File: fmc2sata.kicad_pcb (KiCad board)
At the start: 4 copper layers, 105 x 69 mm, 40 parts, among them J1 ASP-134488-01, J2 1-2199230-6, J3 te-770829-1, U1 TPS565208, U2 TPS565208, Y1 AX3DAF1-150.0000

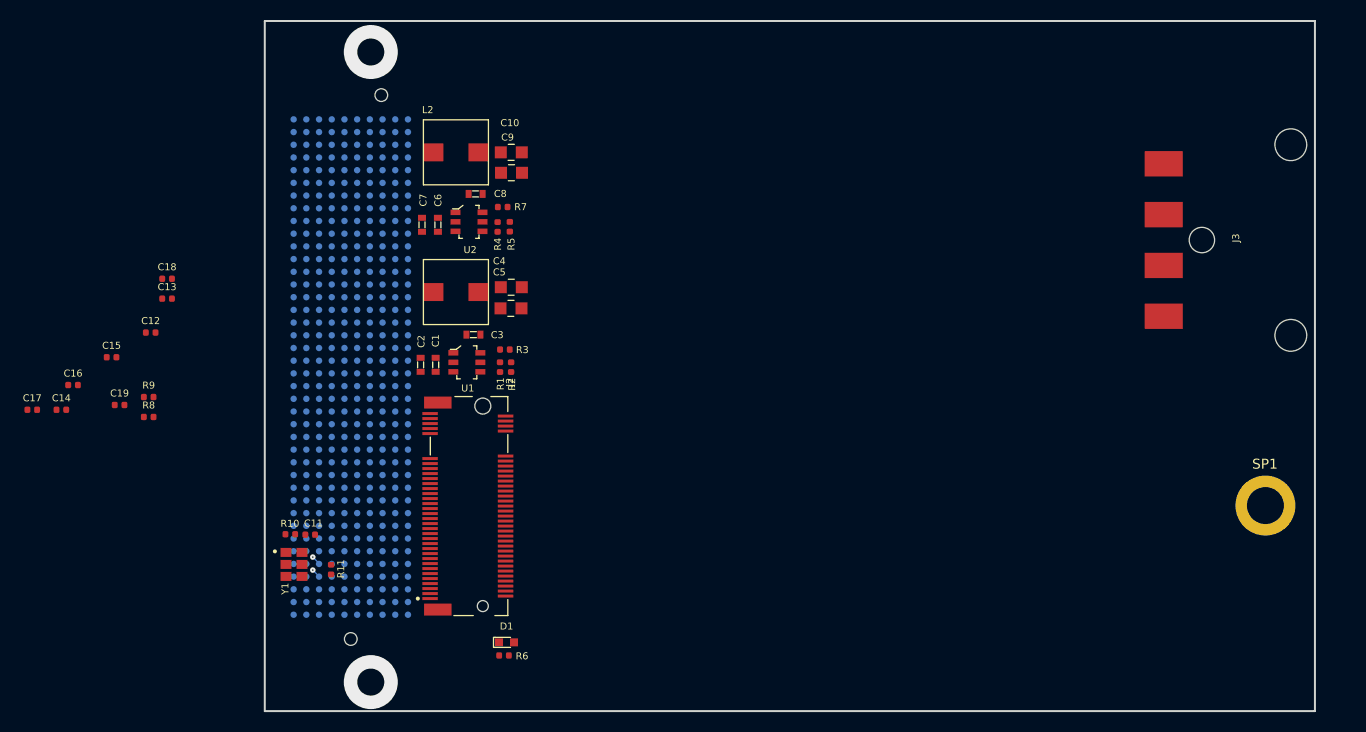
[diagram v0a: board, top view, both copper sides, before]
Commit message: Add board fastening holes
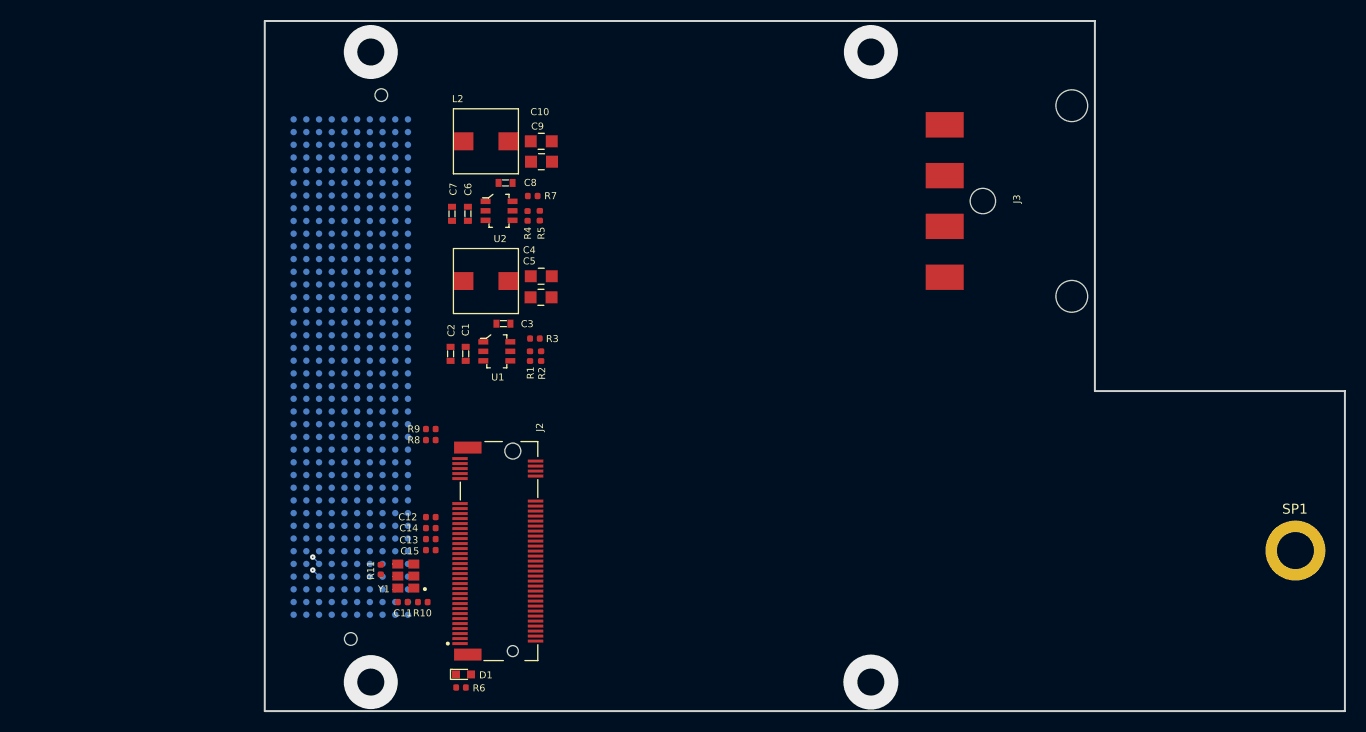
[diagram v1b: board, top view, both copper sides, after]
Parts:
- removed C16, C17, C18, C19: C_10n_0402, antmicro-footprints:0402-cap
- moved C14 38.8 mm to (88.6, 93.7)
- moved C15 37.3 mm to (88.6, 95.9)
- moved C13 35.7 mm to (88.6, 94.8)
- moved C12 33.5 mm to (88.6, 92.6)
- moved R9 28.4 mm to (88.6, 83.8)
- moved R8 28.3 mm to (88.6, 84.9), turned to 180 degrees
- moved J3 22.2 mm to (143.8, 61.0)
- moved R10 14.9 mm to (87.8, 101.1)
- moved C11 11.5 mm to (85.8, 101.1)
- moved Y1 11.2 mm to (86.1, 98.5), turned to 90 degrees
- moved J2 5.41 mm to (96.8, 96.0)
- moved SP1 5.41 mm to (175.0, 96.0)
- moved D1 5.36 mm to (91.9, 108.3)
- moved R6 5.36 mm to (91.6, 109.6)
- moved R11 4.97 mm to (83.6, 97.8), turned to 270 degrees
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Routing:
- net (no net): vias 2 -> 4
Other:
- board size 105 x 69 mm -> 108 x 69 mm

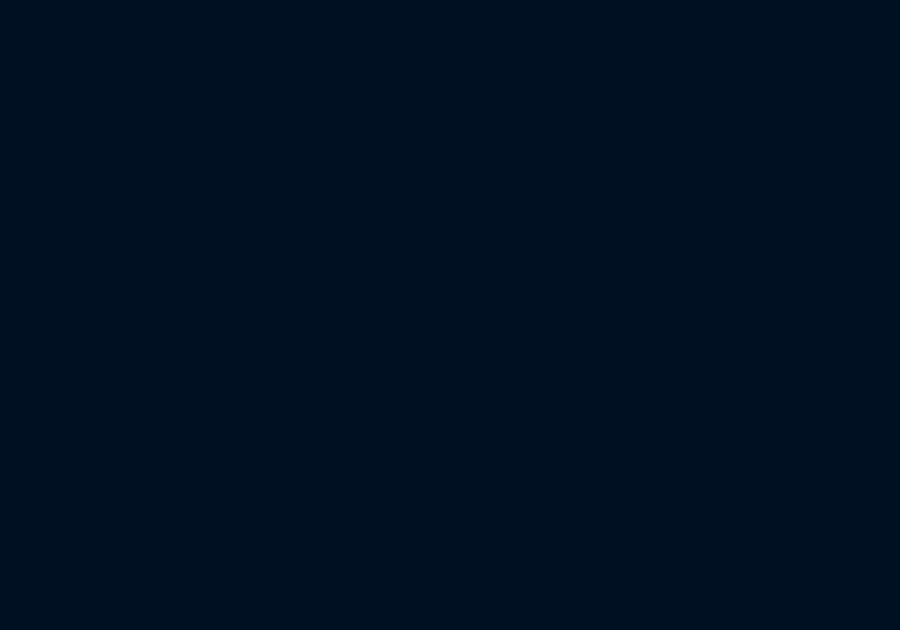
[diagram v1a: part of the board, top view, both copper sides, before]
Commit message: Add second M.2 mouting stud
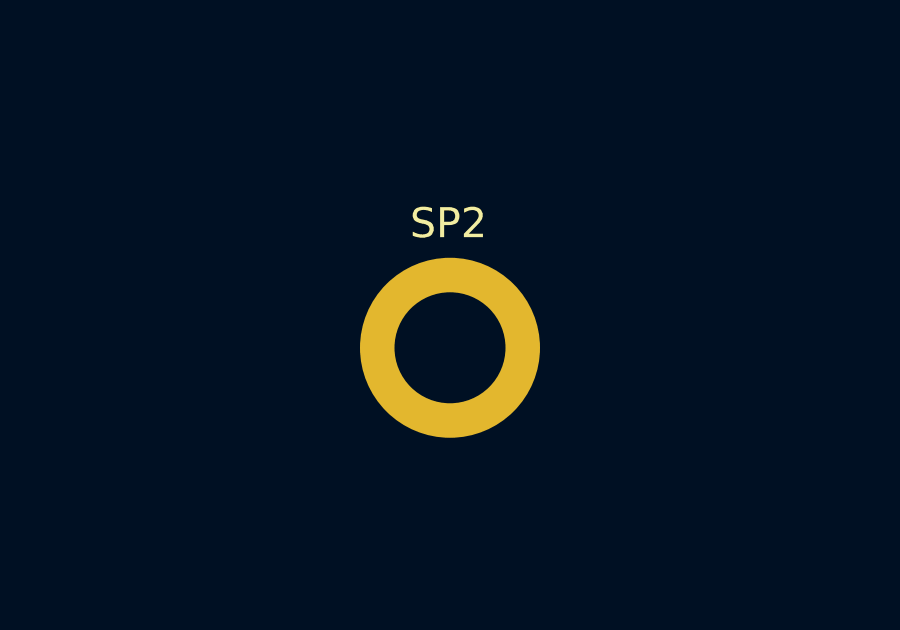
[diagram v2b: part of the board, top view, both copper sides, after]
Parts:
- added SP2: 9774025151, antmicro-footprints:9774025151, F.Cu at (136.8, 96.0)
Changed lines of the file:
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@@
     (tracks 10)
     (zones 0)
-    (modules 36)
+    (modules 37)
     (nets 155)
   )
@@
     (add_net SATA_CLK_P)
   )
+  (module antmicro-footprints:9774025151 (layer F.Cu)
+    (at 136.8 96)
+    (fp_text reference SP2 (at 0 -4.2) (layer F.SilkS)
+      (effects (font (size 1 1) (thickness 0.15)))
+    )
+    (fp_text value 9774025151 (at -0.05 4.35) (layer F.Fab)
+      (effects (font (size 1 1) (thickness 0.15)))
+    )
+    (pad 1 thru_hole circle (at 0.05 -0.05) (size 6 6) (drill 3.7) (layers *.Cu F.SilkS F.Mask)
+      (net 2 GND) (solder_paste_margin -1.2))
+    (model ${KIPRJMOD}/lib/3d-models/9774025151.stp
+      (at (xyz 0 0 0))
+      (scale (xyz 1 1 1))
+      (rotate (xyz 0 0 0))
+    )
+  )
   (module antmicro-footprints:9774025151 locked (layer F.Cu)
     (at 175 96)
@@
     )
   )
-  (module antmicro-footprints:1-2199230-6 locked (layer F.Cu)
+  (module antmicro-footprints:1-2199230-6 (layer F.Cu)
     (at 96.8 96 90)
     (fp_text reference J2 (at 12.38 2.69 90) (layer F.SilkS)

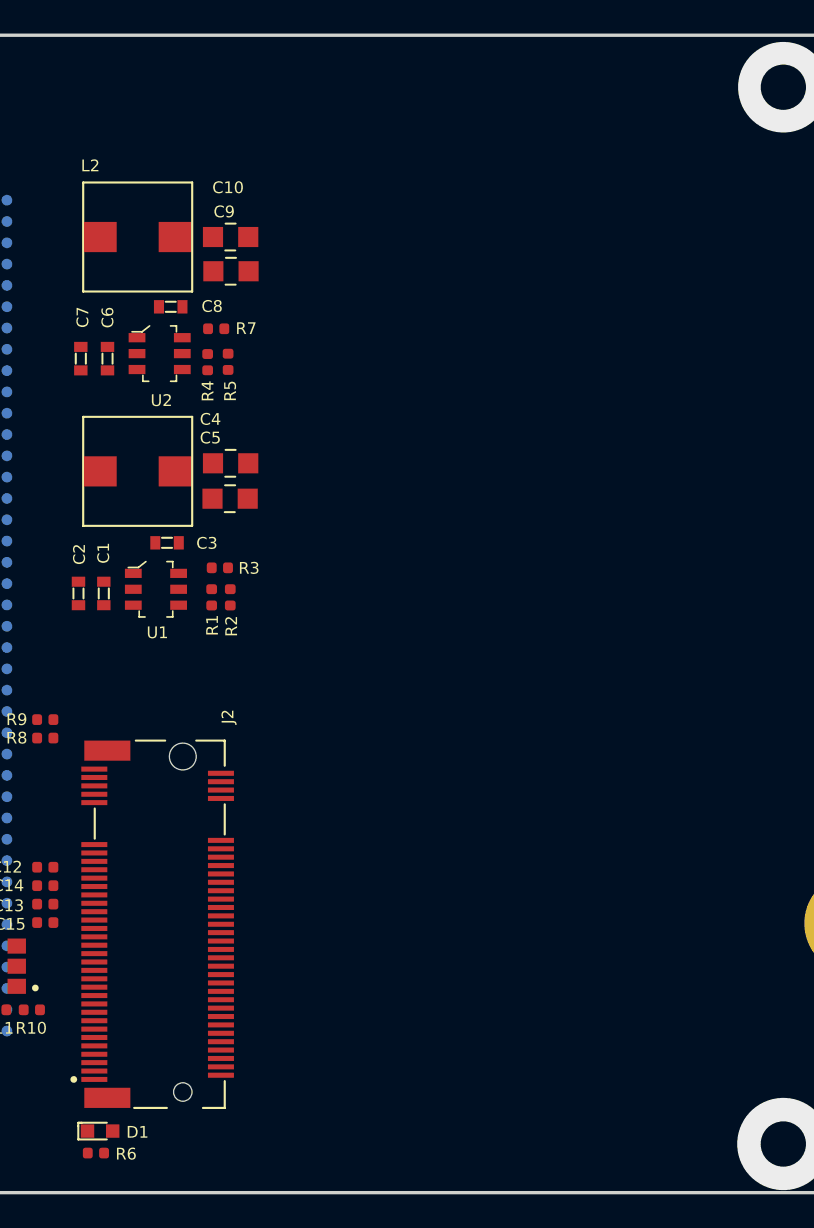
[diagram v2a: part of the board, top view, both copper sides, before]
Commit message: Add PWR indicators
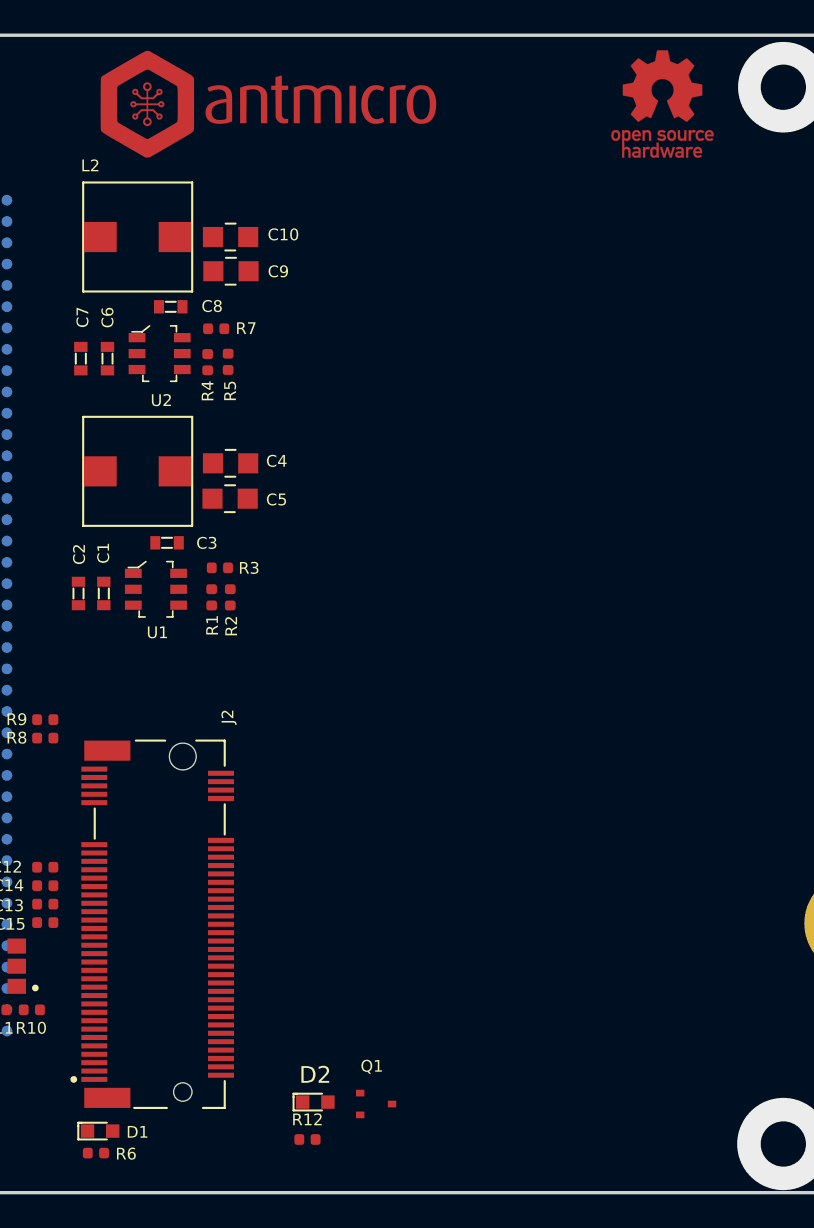
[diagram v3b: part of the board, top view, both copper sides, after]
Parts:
- added D2: LTST-C191KRKT, antmicro-footprints:LED_0603, F.Cu at (104.7, 106.6)
- added N1: antmicro_logo, antmicro-footprints:antmicro-logo_scaled_20mm, F.Cu at (101.9, 47.3)
- added N2: oshw_logo, antmicro-footprints:oshw-logo, F.Cu at (125.4, 47.1)
- added Q1: BSS138APW, antmicro-footprints:SC70-3, F.Cu at (108.3, 106.7)
- added R12: R_0R_0402, antmicro-footprints:0402-res, F.Cu at (104.2, 108.8)
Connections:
- J2 pad 69: Net-(J2-Pad69) -> SATA_FLAG
- R8 pad 1: +3V3 -> VCC_IO
- R8 pad 2: Net-(J2-Pad69) -> SATA_FLAG
- R9 pad 1: Net-(J2-Pad69) -> Net-(J1-PadH14)

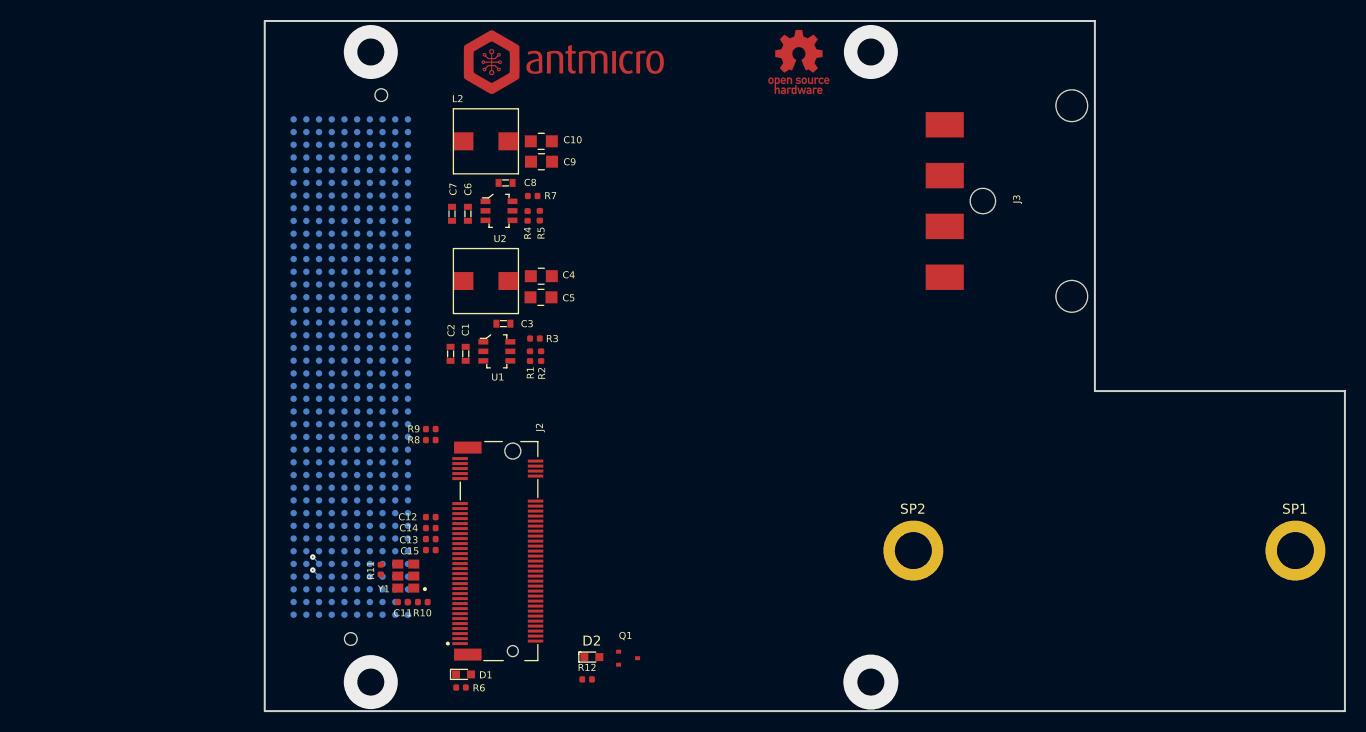
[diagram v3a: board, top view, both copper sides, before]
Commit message: Update compoent placement
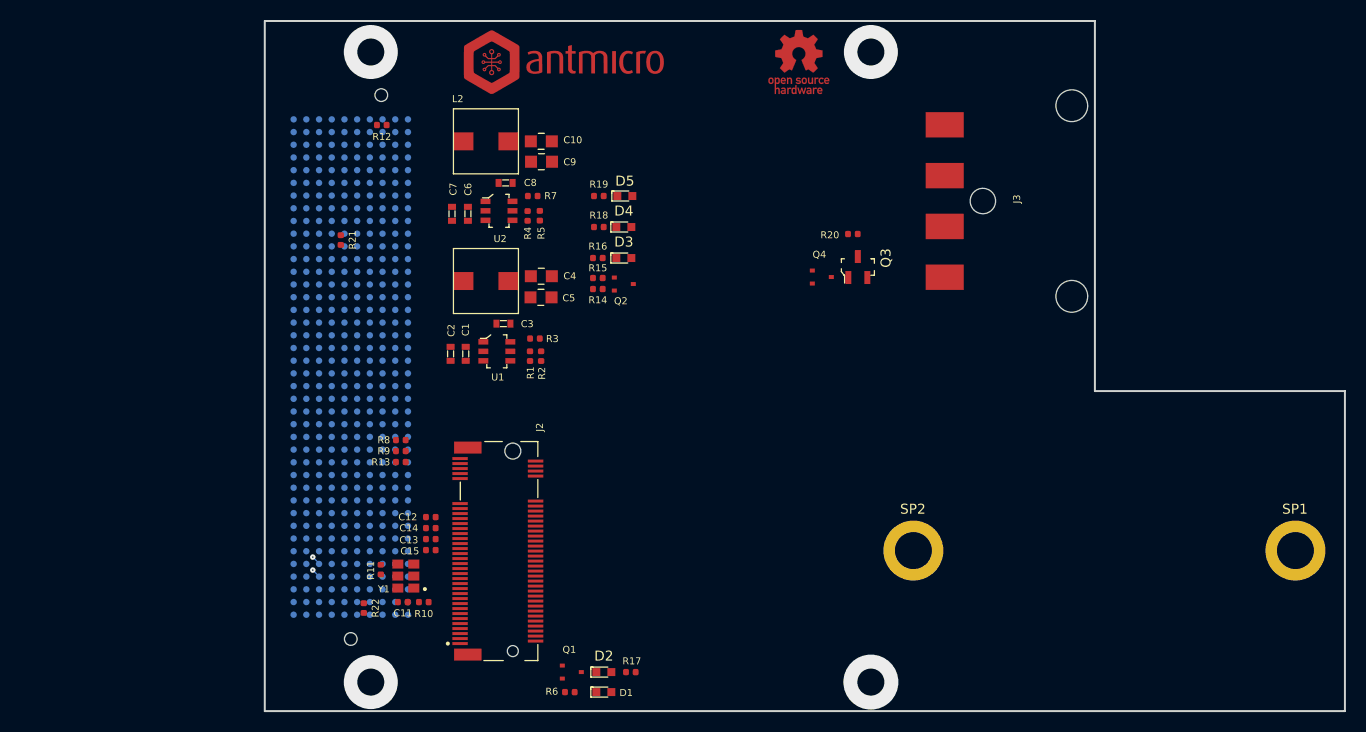
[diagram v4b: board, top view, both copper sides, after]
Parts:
- added D3: KP-1608CGCK, antmicro-footprints:LED_0603, F.Cu at (107.9, 66.7)
- added D4: KP-1608CGCK, antmicro-footprints:LED_0603, F.Cu at (107.9, 63.6)
- added D5: KP-1608CGCK, antmicro-footprints:LED_0603, F.Cu at (108.0, 60.5)
- added Q2: BSS138APW, antmicro-footprints:SC70-3, F.Cu at (107.9, 69.3)
- added Q3: DMG2305UX-13, antmicro-footprints:SOT-23-3, F.Cu at (131.3, 67.6)
- added Q4: BSS138APW, antmicro-footprints:SC70-3, F.Cu at (127.7, 68.6)
- added R13: R_0R_0402, antmicro-footprints:0402-res, F.Cu at (85.6, 87.1)
- added R14: R_10k_0402, antmicro-footprints:0402-res, F.Cu at (105.3, 69.8)
- added R15: R_10k_0402, antmicro-footprints:0402-res, F.Cu at (105.3, 68.7)
- added R16: R_1k1_0402, antmicro-footprints:0402-res, F.Cu at (105.3, 66.7)
- added R17: R_330R_0402, antmicro-footprints:0402-res, F.Cu at (108.6, 108.1)
- added R18: R_330R_0402, antmicro-footprints:0402-res, F.Cu at (105.4, 63.6)
- added R19: R_330R_0402, antmicro-footprints:0402-res, F.Cu at (105.4, 60.5)
- added R20: R_10k_0402, antmicro-footprints:0402-res, F.Cu at (130.8, 64.3)
- added R21: R_0R_0402, antmicro-footprints:0402-res, F.Cu at (79.6, 64.9)
- added R22: R_0R_0402, antmicro-footprints:0402-res, F.Cu at (81.9, 101.7)
- R10: value R_1k_0402 -> R_10k_0402
- moved R12 59.1 mm to (83.7, 53.4), turned to 180 degrees
- moved D1 14.1 mm to (105.9, 110.1)
- moved R6 10.9 mm to (102.5, 110.1), turned to 0 degrees
- moved Q1 5.79 mm to (102.7, 108.1)
- moved R9 3.72 mm to (85.6, 86.0)
- moved R8 3.00 mm to (85.6, 84.9), turned to 0 degrees
- moved D2 1.92 mm to (105.9, 108.1)
- moved R10 0.10 mm to (87.9, 101.1)
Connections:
- J1 pad D30: Net-(J1-PadD30) -> /JTAG_TDI
- J1 pad D31: Net-(J1-PadD31) -> /JTAG_TDO
- J1 pad H2: Net-(J1-PadH2) -> /PRSNT
- J3 pad 1: +12V -> Net-(J3-Pad1)
- Q1 pad 1: Net-(Q1-Pad1) -> SATA_FLAG
- Q1 pad 2: Net-(Q1-Pad2) -> GND
- Q1 pad 3: Net-(Q1-Pad3) -> Net-(D2-Pad1)
- R10 pad 1: +3V3 -> Net-(R10-Pad1)
- R10 pad 2: Net-(R10-Pad2) -> +3V3
- Y1 pad 1: Net-(R10-Pad2) -> Net-(R10-Pad1)
